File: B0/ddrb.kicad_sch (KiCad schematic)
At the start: 4 parts, among them U001 74HCT00, U005 74HCT244, U007 74HCT32, U025 74HCT377

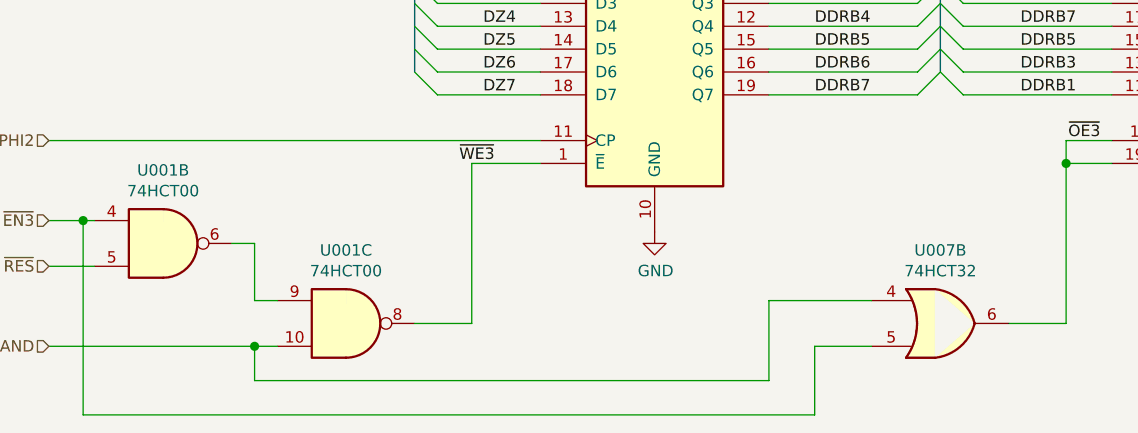
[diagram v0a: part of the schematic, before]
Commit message: B1 CREGA added
Work started on b1. CREGA added.
Minor changes to B0 schematic properties.
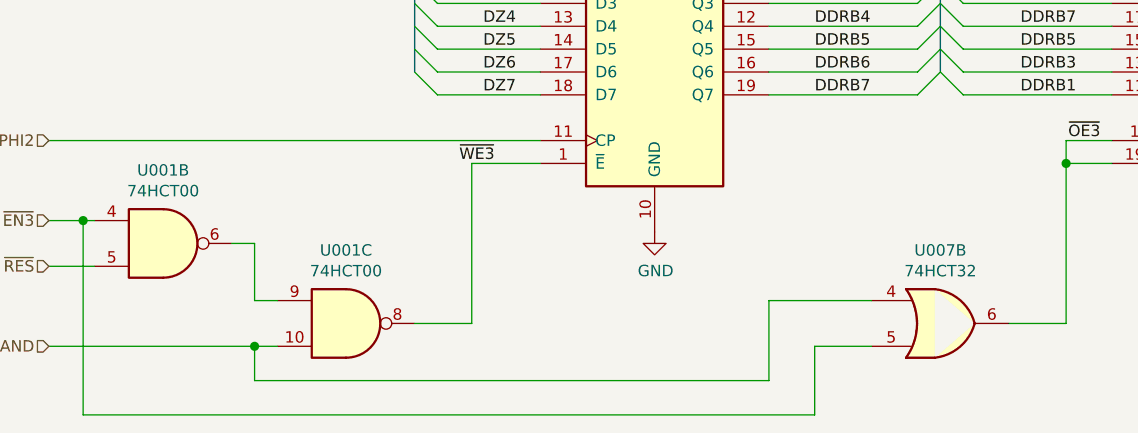
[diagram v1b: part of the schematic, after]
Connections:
- net ~EN3 renamed ~{EN3}
- net ~OE3 renamed ~{OE3}
- net ~RES renamed ~{RES}
- net ~WE3 renamed ~{WE3}

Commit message: .
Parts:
- U005: value 74HCT244 -> 74HC244
- U007: value 74HCT32 -> 74HC32
- U025: value 74HCT377 -> 74HC377
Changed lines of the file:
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@@
     (in_bom yes) (on_board yes)
     (property "Reference" "U007" (id 0) (at 158.75 103.6382 0))
-    (property "Value" "74HCT32" (id 1) (at 158.75 105.9369 0))
+    (property "Value" "74HC32" (id 1) (at 158.75 105.9369 0))
     (property "Footprint" "74hct6526.footprints:SO-14" (id 2) (at 158.75 111.76 0)
       (effects (font (size 1.27 1.27)) hide)
@@
     (in_bom yes) (on_board yes)
     (property "Reference" "U025" (id 0) (at 133.35 60.3058 0))
-    (property "Value" "74HCT377" (id 1) (at 133.35 62.6045 0))
+    (property "Value" "74HC377" (id 1) (at 133.35 62.6045 0))
     (property "Footprint" "74hct6526.footprints:SOIC-20W" (id 2) (at 127 81.28 0)
       (effects (font (size 1.27 1.27)) hide)
@@
     (in_bom yes) (on_board yes)
     (property "Reference" "U005" (id 0) (at 198.12 60.3058 0))
-    (property "Value" "74HCT244" (id 1) (at 198.12 62.6045 0))
+    (property "Value" "74HC244" (id 1) (at 198.12 62.6045 0))
     (property "Footprint" "74hct6526.footprints:SOIC-20W" (id 2) (at 190.5 81.28 0)
       (effects (font (size 1.27 1.27)) hide)
